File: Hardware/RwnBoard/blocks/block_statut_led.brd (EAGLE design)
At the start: 100 x 80 mm, 8 parts

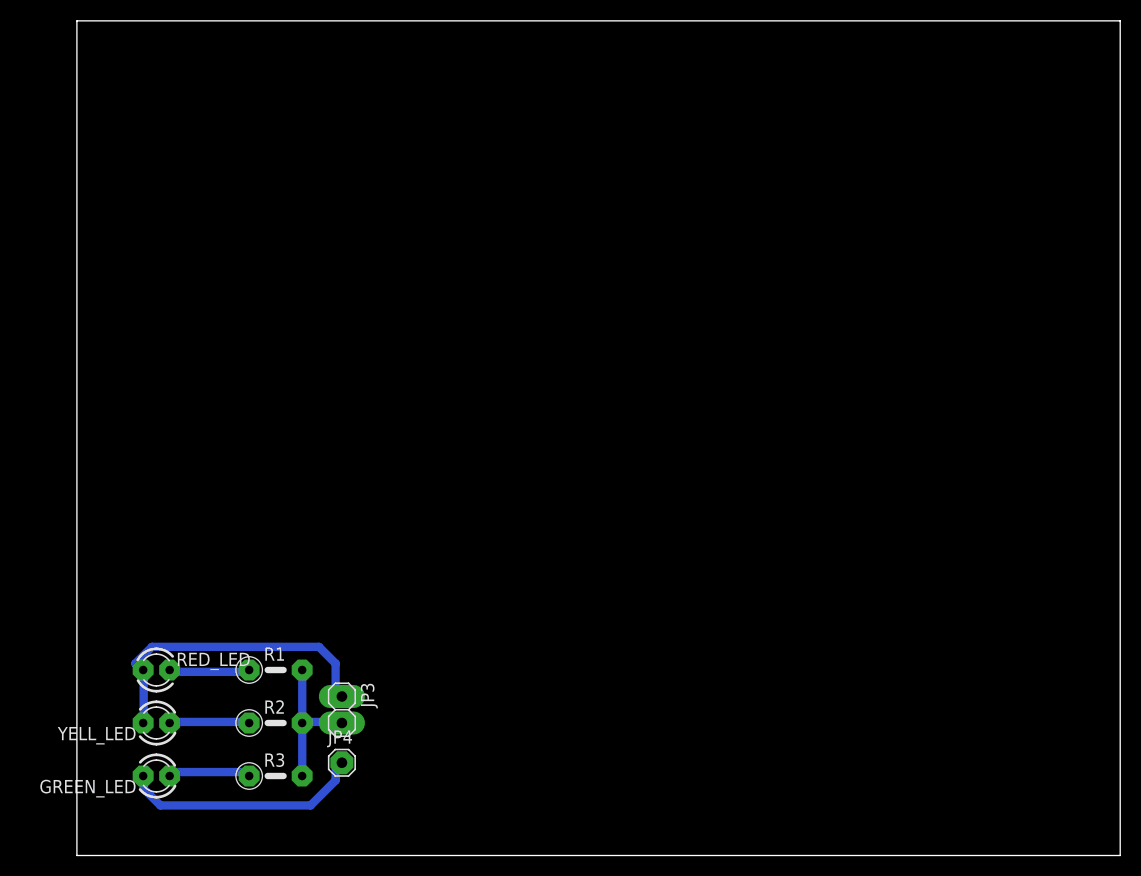
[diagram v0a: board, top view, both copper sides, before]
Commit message: -Reduce "block_statut_led" layout size for 3D preview -Add images as wiki ,gitPages ressources
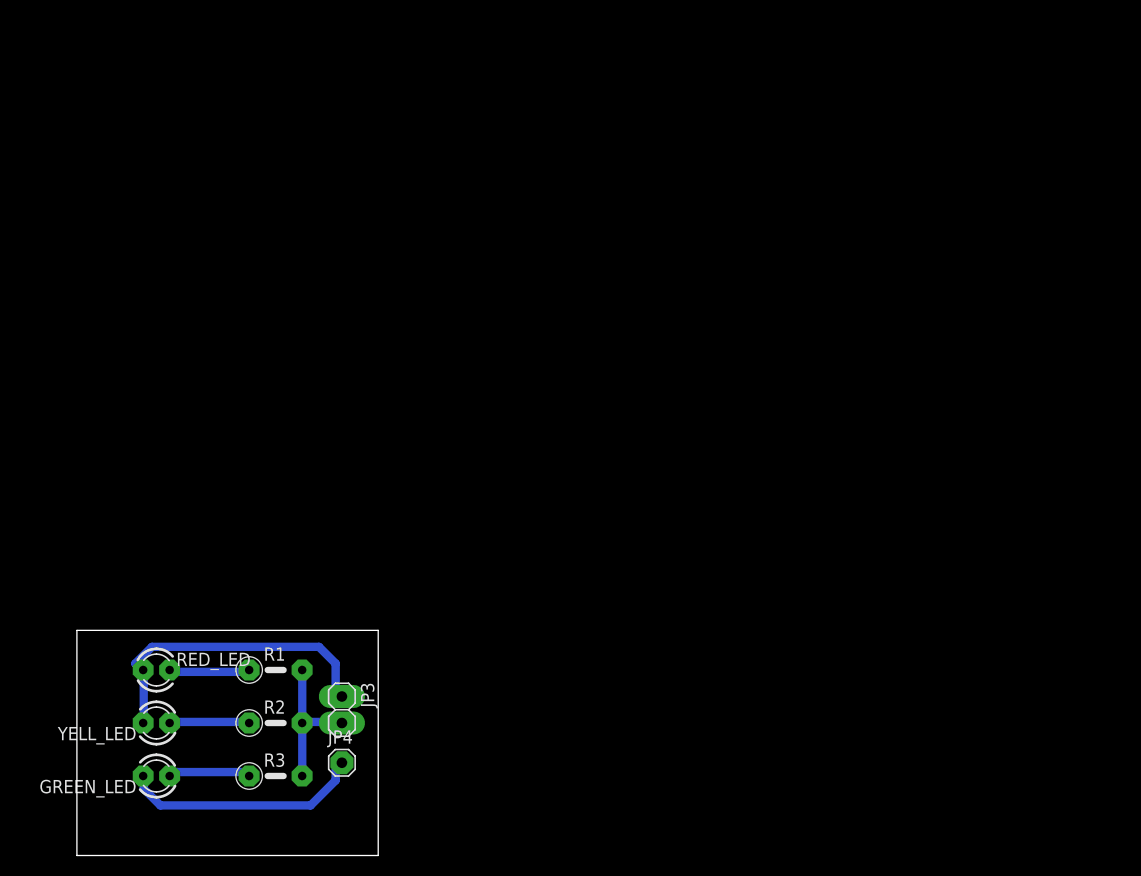
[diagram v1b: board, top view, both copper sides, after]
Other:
- board size 100 x 80 mm -> 28.9 x 21.6 mm
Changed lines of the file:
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@@
 <board>
 <plain>
-<wire x1="0" y1="0" x2="100" y2="0" width="0" layer="20"/>
-<wire x1="100" y1="0" x2="100" y2="80" width="0" layer="20"/>
-<wire x1="100" y1="80" x2="0" y2="80" width="0" layer="20"/>
-<wire x1="0" y1="80" x2="0" y2="0" width="0" layer="20"/>
+<wire x1="0" y1="0" x2="28.88" y2="0" width="0" layer="20"/>
+<wire x1="28.88" y1="0" x2="28.88" y2="21.58" width="0" layer="20"/>
+<wire x1="28.88" y1="21.58" x2="0" y2="21.58" width="0" layer="20"/>
+<wire x1="0" y1="21.58" x2="0" y2="0" width="0" layer="20"/>
 </plain>
 <attributes>
